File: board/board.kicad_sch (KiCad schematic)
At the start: 1 part, among them J1 009_1000BASE-T

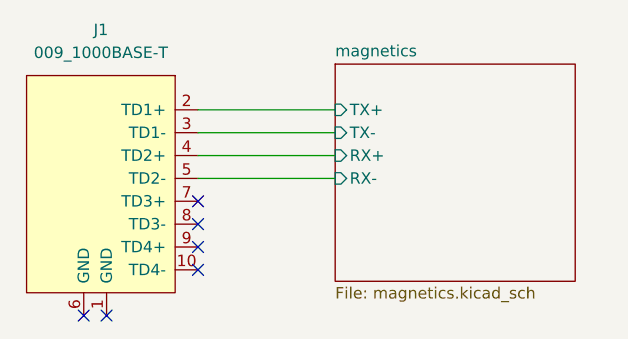
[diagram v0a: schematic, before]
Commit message: changed subsheet name
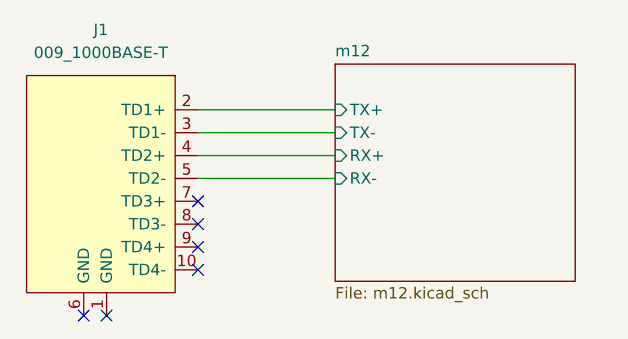
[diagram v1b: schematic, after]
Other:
- sheet magnetics renamed m12
- sheet m12: file magnetics.kicad_sch -> m12.kicad_sch
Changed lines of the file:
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@@
     (stroke (width 0.1524) (type solid) (color 0 0 0 0))
     (fill (color 0 0 0 0.0000))
-    (property "Sheet name" "magnetics" (id 0) (at 116.84 81.8384 0)
+    (property "Sheet name" "m12" (id 0) (at 116.84 81.8384 0)
       (effects (font (size 1.27 1.27)) (justify left bottom))
     )
-    (property "Sheet file" "magnetics.kicad_sch" (id 1) (at 116.84 107.2646 0)
+    (property "Sheet file" "m12.kicad_sch" (id 1) (at 116.84 107.2646 0)
       (effects (font (size 1.27 1.27)) (justify left top))
     )
